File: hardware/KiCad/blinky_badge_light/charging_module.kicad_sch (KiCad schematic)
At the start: 8 parts, among them U2 TP4056

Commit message: updates to hardware schematic
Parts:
- U2: footprint SOP8-PP_TPW -> footprints:SOP8-PP_TPW
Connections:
- net at R14.2: now also D25.2 (A); no longer D25.1 (K)
- net at U2.7 (*CHRG): now also D25.1 (K); no longer D25.2 (A)
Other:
- moved on the sheet: D25

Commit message: stuff from today
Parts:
- C32, C33: footprint Capacitor_SMD:C_0201_0603Metric -> Capacitor_SMD:C_0603_1608Metric
- R4: footprint Resistor_SMD:R_0201_0603Metric -> Resistor_SMD:R_0603_1608Metric
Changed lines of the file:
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@@
 			)
 		)
-		(property "Footprint" "Capacitor_SMD:C_0201_0603Metric"
+		(property "Footprint" "Capacitor_SMD:C_0603_1608Metric"
 			(at 193.04 59.9948 0)
 			(effects
@@
 			)
 		)
-		(property "Footprint" "Capacitor_SMD:C_0201_0603Metric"
+		(property "Footprint" "Capacitor_SMD:C_0603_1608Metric"
 			(at 157.7848 115.57 0)
 			(effects
@@
 			)
 		)
-		(property "Footprint" "Resistor_SMD:R_0201_0603Metric"
+		(property "Footprint" "Resistor_SMD:R_0603_1608Metric"
 			(at 170.18 95.758 90)
 			(effects

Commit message: updated schematic to use 'basic' parts from jlcpcb where I could
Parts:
- R4: JLCPCB Part # C22765 -> C22764
- U2: JLCPCB Part # C382139 -> C16581
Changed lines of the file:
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@@
 			)
 		)
-		(property "Datasheet" "https://www.lcsc.com/datasheet/lcsc_datasheet_2206010130_UNI-ROYAL-Uniroyal-Elec-0603WAF1201T5E_C22765.pdf"
+		(property "Datasheet" "https://jlcpcb.com/api/file/downloadByFileSystemAccessId/8579706389601501184"
 			(at 170.18 93.98 0)
 			(effects
@@
 			)
 		)
-		(property "JLCPCB Part #" "C22765"
+		(property "JLCPCB Part #" "C22764"
 			(at 170.18 93.98 90)
 			(effects
@@
 			)
 		)
-		(property "Datasheet" "https://www.lcsc.com/datasheet/lcsc_datasheet_1912111437_TPOWER-TP4056_C382139.pdf"
+		(property "Datasheet" "https://jlcpcb.com/api/file/downloadByFileSystemAccessId/8588879072461508608"
 			(at 165.1 96.52 0)
 			(effects
@@
 			)
 		)
-		(property "JLCPCB Part #" "C382139"
+		(property "JLCPCB Part #" "C16581"
 			(at 165.1 96.52 0)
 			(effects

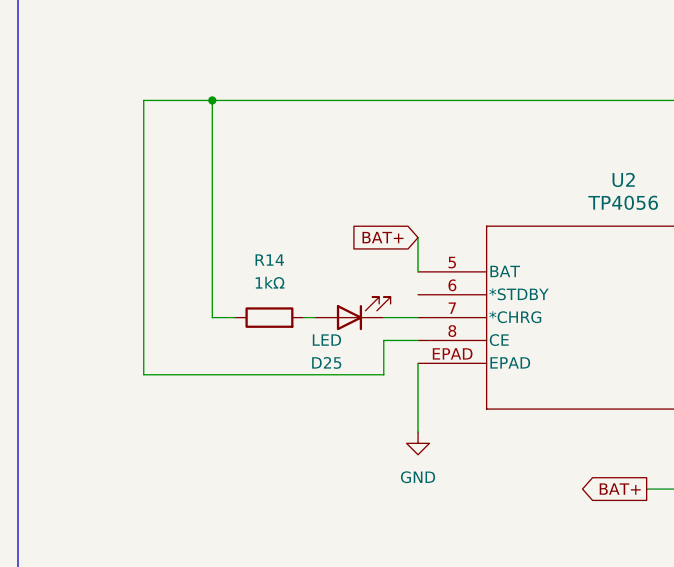
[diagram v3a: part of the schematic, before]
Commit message: charging led is too bright, swapped resistor from 1k to 3k
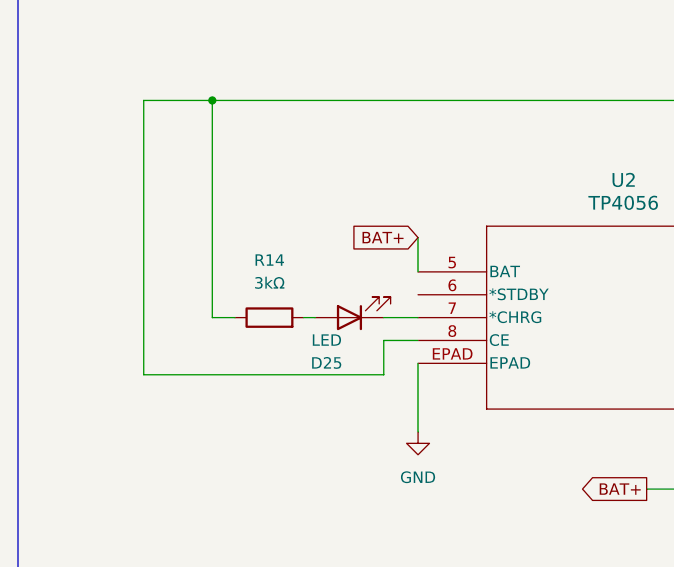
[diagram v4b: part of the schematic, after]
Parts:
- R14: value 1kΩ -> 3kΩ; JLCPCB Part # C21190 -> C4211
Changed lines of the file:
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@@
 			)
 		)
-		(property "Value" "1kΩ"
+		(property "Value" "3kΩ"
 			(at 102.87 87.63 90)
 			(effects
@@
 			)
 		)
-		(property "Datasheet" "https://www.lcsc.com/datasheet/lcsc_datasheet_2206010130_UNI-ROYAL-Uniroyal-Elec-0603WAF1001T5E_C21190.pdf"
+		(property "Datasheet" "https://jlcpcb.com/api/file/downloadByFileSystemAccessId/8579706243143307264"
 			(at 102.87 91.44 0)
 			(effects
@@
 			)
 		)
-		(property "JLCPCB Part #" "C21190"
+		(property "JLCPCB Part #" "C4211"
 			(at 102.87 91.44 90)
 			(effects

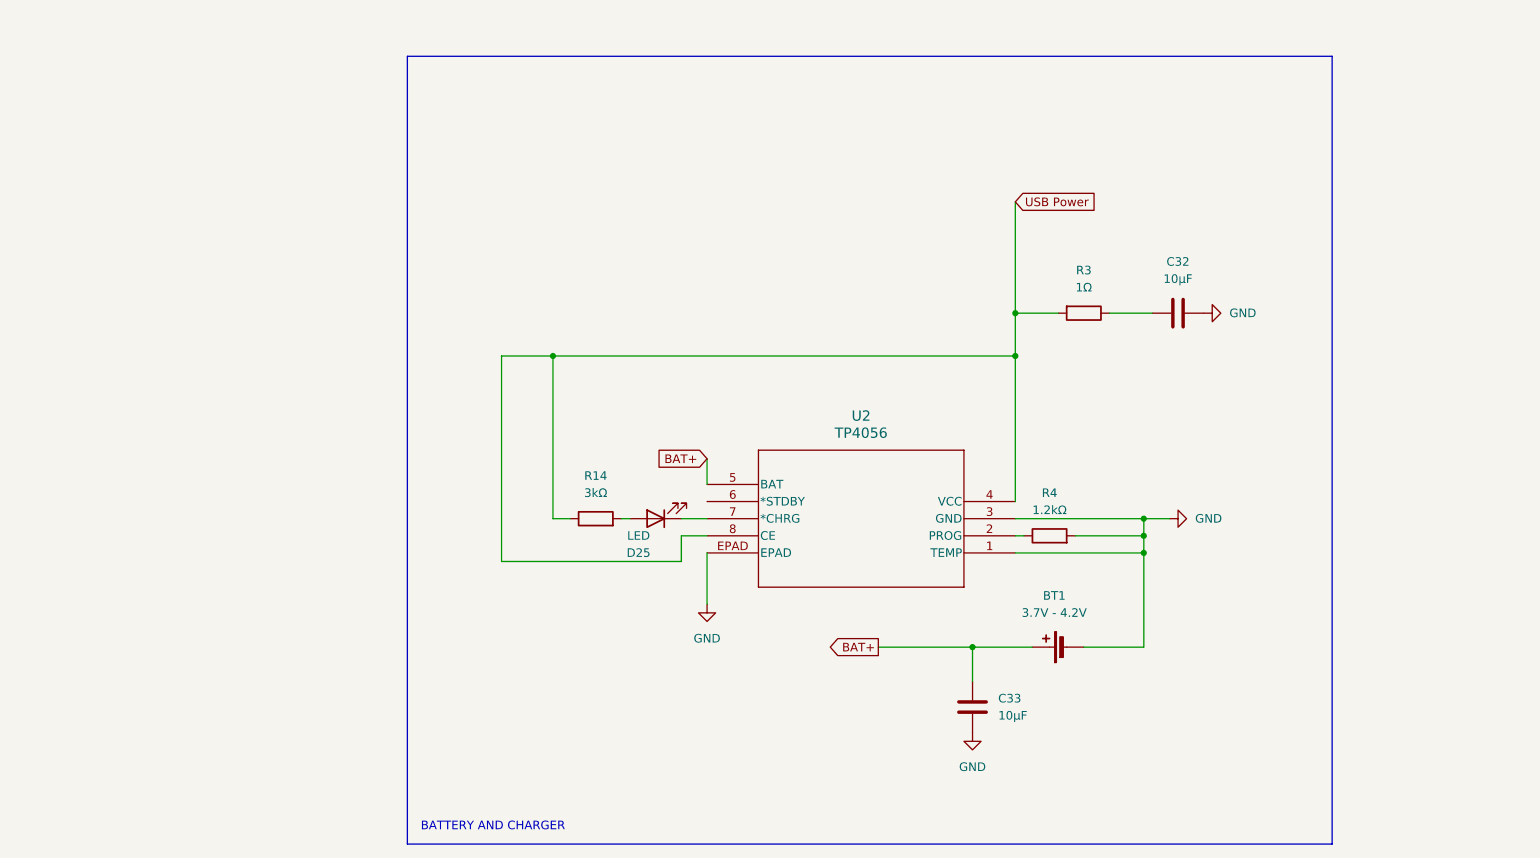
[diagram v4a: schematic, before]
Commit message: added battery polarity protection and charging monitoring circuit
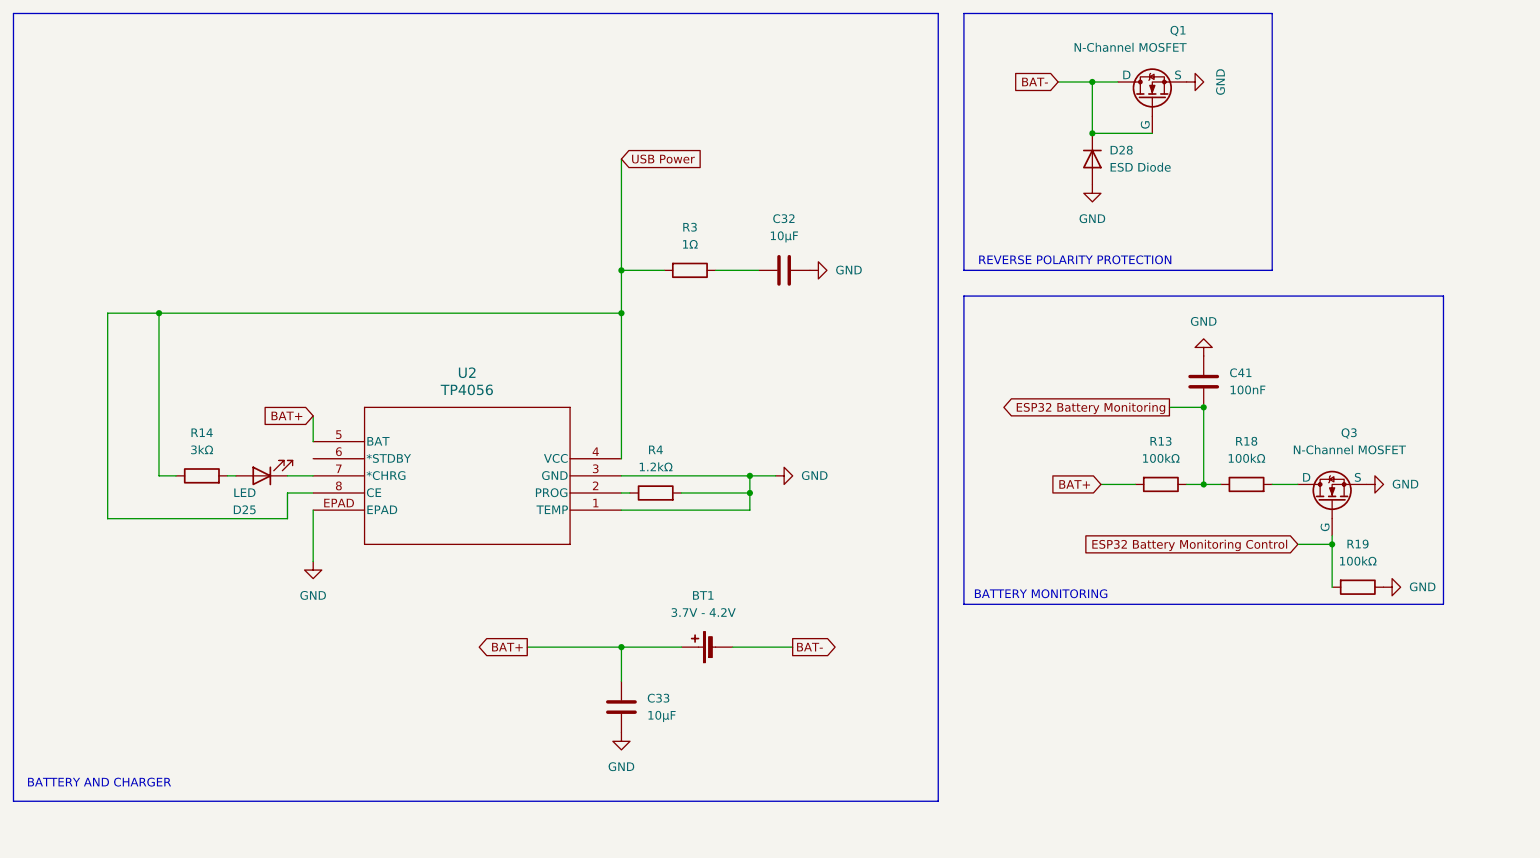
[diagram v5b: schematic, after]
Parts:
- added C41: 100nF, Capacitor_SMD:C_0402_1005Metric, symbol Device:C
- added D28: ESD Diode, Diode_SMD:D_SOD-123, symbol Device:D
- added Q1, Q3: N-Channel MOSFET, footprints:SOT-23-3_L2.9-W1.3-P1.90-LS2.4-BR, symbol Simulation_SPICE:NMOS
- added R13, R18, R19: 100kΩ, Resistor_SMD:R_0603_1608Metric, symbol Device:R
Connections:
- net BAT+: now also R13.2
- net GND: now also C41.1, D28.2 (A), Q1.3 (S), Q3.3 (S), R19.1; no longer BT1.2 (-)
- new net: Q3.1 (D), R18.2
- new net BAT-: BT1.2 (-), D28.1 (K), Q1.1 (D), Q1.2 (G)
- new net ESP32 Battery Monitoring: C41.2, R13.1, R18.1
- new net ESP32 Battery Monitoring Control: Q3.2 (G), R19.2
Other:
- note added: "BATTERY MONITORING"
- note added: "REVERSE POLARITY PROTECTION"
- moved on the sheet: BT1, C32, C33, D25, R14, R3, R4, U2

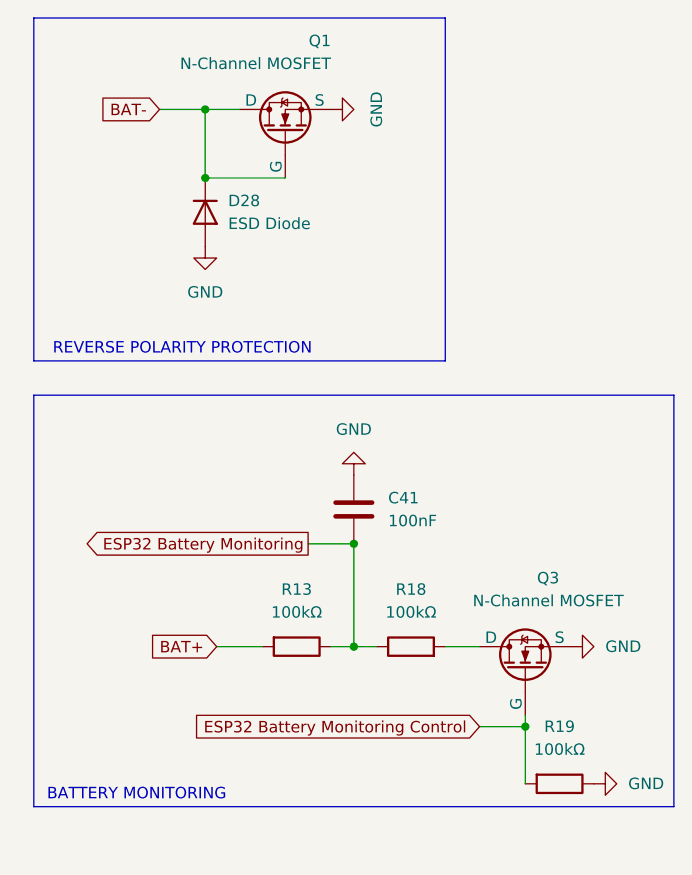
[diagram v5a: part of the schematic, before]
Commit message: fix symbol used by transistor
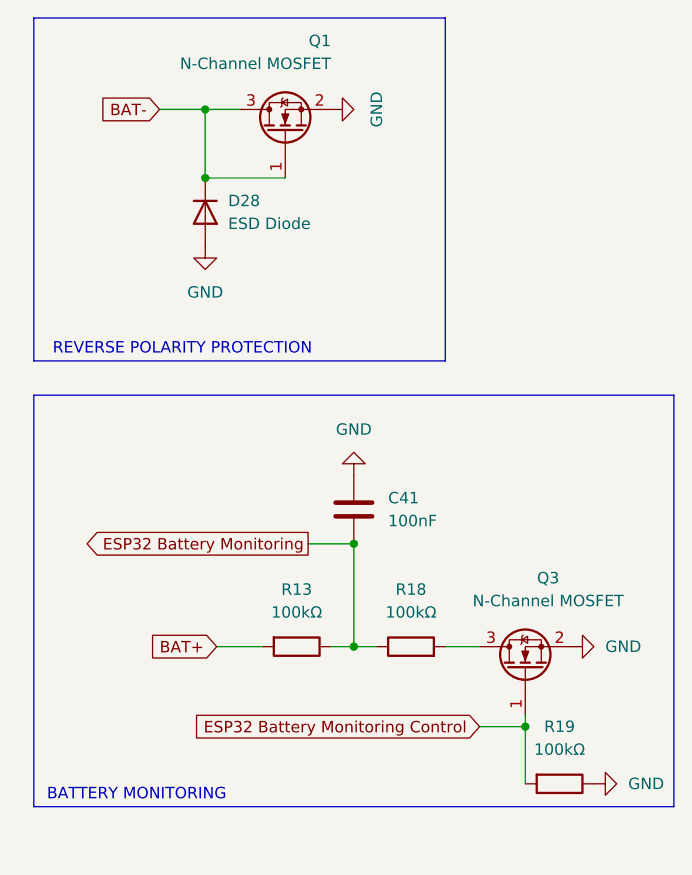
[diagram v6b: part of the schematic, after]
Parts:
- Q1, Q3: symbol Simulation_SPICE:NMOS -> Transistor_FET:AO3400A
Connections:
- net BAT-: now also Q1.3 (D); no longer Q1.2 (G)
- net ESP32 Battery Monitoring Control: now also Q3.1 (G); no longer Q3.2 (G)
- net GND: now also Q1.2 (S), Q3.2 (S); no longer Q1.3 (S), Q3.3 (S)
- net at R18.2: now also Q3.3 (D); no longer Q3.1 (D)
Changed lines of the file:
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@@
 	)
 	(symbol
-		(lib_id "Simulation_SPICE:NMOS")
+		(lib_id "Transistor_FET:AO3400A")
 		(at 185.42 29.21 90)
 		(unit 1)
@@
 		)
 		(property "Footprint" "footprints:SOT-23-3_L2.9-W1.3-P1.90-LS2.4-BR"
-			(at 182.88 24.13 0)
-			(effects
-				(font
-					(size 1.27 1.27)
-				)
-				(hide yes)
-			)
-		)
-		(property "Datasheet" "https://jlcpcb.com/api/file/downloadByFileSystemAccessId/8550723985357750272"
-			(at 198.12 29.21 0)
-			(effects
-				(font
-					(size 1.27 1.27)
-				)
-				(hide yes)
-			)
-		)
-		(property "Description" "N-MOSFET transistor, drain/source/gate"
+			(at 187.325 24.13 0)
+			(effects
+				(font
+					(size 1.27 1.27)
+					(italic yes)
+				)
+				(justify left)
+				(hide yes)
+			)
+		)
+		(property "Datasheet" "http://www.aosmd.com/pdfs/datasheet/AO3400A.pdf"
+			(at 189.23 24.13 0)
+			(effects
+				(font
+					(size 1.27 1.27)
+				)
+				(justify left)
+				(hide yes)
+			)
+		)
+		(property "Description" "30V Vds, 5.7A Id, N-Channel MOSFET, SOT-23"
+			(at 185.42 29.21 0)
+			(effects
+				(font
+					(size 1.27 1.27)
+				)
+				(hide yes)
+			)
+		)
+		(property "JLCBCB Part #" "C20917"
 			(at 185.42 29.21 0)
 			(effects
@@
 			)
 		)
-		(property "Sim.Pins" "1=D 2=G 3=S"
+		(property "Sim.Pins" "1=G 2=S 3=D"
 			(at 200.66 29.21 0)
-			(effects
-				(font
-					(size 1.27 1.27)
-				)
-				(hide yes)
-			)
-		)
-		(property "JLCBCB Part #" "C20917"
-			(at 185.42 29.21 0)
 			(effects
 				(font
@@
 	)
 	(symbol
-		(lib_id "Simulation_SPICE:NMOS")
+		(lib_id "Transistor_FET:AO3400A")
 		(at 212.09 88.9 90)
 		(unit 1)
@@
 		)
 		(property "Footprint" "footprints:SOT-23-3_L2.9-W1.3-P1.90-LS2.4-BR"
-			(at 209.55 83.82 0)
-			(effects
-				(font
-					(size 1.27 1.27)
-				)
-				(hide yes)
-			)
-		)
-		(property "Datasheet" "https://jlcpcb.com/api/file/downloadByFileSystemAccessId/8550723985357750272"
-			(at 224.79 88.9 0)
-			(effects
-				(font
-					(size 1.27 1.27)
-				)
-				(hide yes)
-			)
-		)
-		(property "Description" "N-MOSFET transistor, drain/source/gate"
+			(at 213.995 83.82 0)
+			(effects
+				(font
+					(size 1.27 1.27)
+					(italic yes)
+				)
+				(justify left)
+				(hide yes)
+			)
+		)
+		(property "Datasheet" "http://www.aosmd.com/pdfs/datasheet/AO3400A.pdf"
+			(at 215.9 83.82 0)
+			(effects
+				(font
+					(size 1.27 1.27)
+				)
+				(justify left)
+				(hide yes)
+			)
+		)
+		(property "Description" "30V Vds, 5.7A Id, N-Channel MOSFET, SOT-23"
 			(at 212.09 88.9 0)
 			(effects
@@
 			)
 		)
-		(property "Sim.Pins" "1=D 2=G 3=S"
+		(property "Sim.Pins" "3=D 1=G 2=S"
 			(at 227.33 88.9 0)
 			(effects
